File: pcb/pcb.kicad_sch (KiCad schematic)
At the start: 97 parts, among them J1 MJ-4PP-9, J2 MJ-4PP-9, J3 USB_C_Receptacle_USB2.0_16P, SW1 KEY_SW, SW10 KEY_SW, SW11 KEY_SW, SW12 KEY_SW, SW13 KEY_SW, SW14 KEY_SW, SW15 KEY_SW, SW16 KEY_SW, SW17 KEY_SW, SW18 KEY_SW, SW19 KEY_SW, SW2 KEY_SW, SW20 KEY_SW, SW21 KEY_SW, SW22 KEY_SW, SW23 KEY_SW, SW24 KEY_SW, SW25 KEY_SW, SW26 KEY_SW, SW27 RotaryEncoder, SW3 KEY_SW, SW30 KEY_SW, SW31 KEY_SW, SW32 KEY_SW, SW33 KEY_SW, SW34 KEY_SW, SW35 KEY_SW, SW36 KEY_SW, SW37 KEY_SW, SW38 KEY_SW, SW39 KEY_SW, SW4 KEY_SW, SW40 KEY_SW, SW41 KEY_SW, SW42 KEY_SW, SW43 KEY_SW, SW44 KEY_SW, SW45 KEY_SW, SW46 KEY_SW, SW47 KEY_SW, SW48 KEY_SW, SW49 KEY_SW, SW5 KEY_SW, SW50 KEY_SW, SW51 KEY_SW, SW52 KEY_SW, SW53 KEY_SW, SW54 KEY_SW, SW55 RotaryEncoder, SW6 KEY_SW, SW60 RESET_SW, SW61 BOOT_SW, SW7 KEY_SW, SW8 KEY_SW, SW9 KEY_SW, U1 ESP32-S3-WROOM-1, U2 TPS1117LV33S, U3 USBLC6-2SC6

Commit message: split connector close #8
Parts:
- added JP1: Jumper_2_Open, symbol Jumper:Jumper_2_Open
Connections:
- net +3V3: now also J2.D; no longer J2.C
- net GND: now also J2.C; no longer J2.D
- net at J1.A: now also J2.A, JP1.1 (A)
- net split-TX: now reaches J2.B
- net split-TX: now also J1.B, U1.10 (IO17)
- net split-RX: now reaches U1.11 (IO18)
- net split-RX: now also JP1.2 (B)
- removed net data: J1.B, J2.A
- no-connect marks 4 -> 3
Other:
- moved on the sheet: J1, J2

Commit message: pcb keyswitch
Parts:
- SW30: footprint keebio:RotaryEncoder_EC11 -> kbd:keyswitch_cherrymx_hotswap_1u
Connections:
- net col0: now also U1.39 (IO1)
- net col1: now also U1.38 (IO2)
- net col2: now also U1.15 (IO3)
- net col3: now also U1.4 (IO4)
- net col4: now also U1.5 (IO5)
- net col5: now also U1.6 (IO6)
- net col6: now also U1.7 (IO7)
- net row0: now also U1.31 (IO38)
- net row1: now also U1.32 (IO39)
- net row2: now also U1.33 (IO40)
- net row3: now also U1.34 (IO41)
- net USB-RX: now reaches U1.36 (RXD0)
- net USB-TX: now reaches U1.37 (TXD0)
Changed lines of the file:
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@@
     (stroke (width 0) (type default))
   )
+  (wire (pts (xy 110.49 197.485) (xy 111.76 197.485))
+    (stroke (width 0) (type default))
+  )
   (wire (pts (xy 260.35 100.33) (xy 260.35 120.65))
     (stroke (width 0) (type default))
@@
     (stroke (width 0) (type default))
   )
+  (wire (pts (xy 143.51 220.345) (xy 142.24 220.345))
+    (stroke (width 0) (type default))
+  )
   (wire (pts (xy 71.12 180.34) (xy 71.12 178.435))
     (stroke (width 0) (type default))
@@
     (stroke (width 0) (type default))
   )
+  (wire (pts (xy 110.49 205.105) (xy 111.76 205.105))
+    (stroke (width 0) (type default))
+  )
   (wire (pts (xy 184.15 68.58) (xy 184.15 88.9))
     (stroke (width 0) (type default))
@@
     (stroke (width 0) (type default))
   )
+  (wire (pts (xy 110.49 210.185) (xy 111.76 210.185))
+    (stroke (width 0) (type default))
+  )
+  (wire (pts (xy 143.51 217.805) (xy 142.24 217.805))
+    (stroke (width 0) (type default))
+  )
   (wire (pts (xy 199.39 107.95) (xy 224.79 107.95))
     (stroke (width 0) (type default))
@@
     (stroke (width 0) (type default))
   )
+  (wire (pts (xy 143.51 189.865) (xy 142.24 189.865))
+    (stroke (width 0) (type default))
+  )
   (wire (pts (xy 173.99 109.855) (xy 148.59 109.855))
     (stroke (width 0) (type default))
@@
     (stroke (width 0) (type default))
   )
+  (wire (pts (xy 143.51 222.885) (xy 142.24 222.885))
+    (stroke (width 0) (type default))
+  )
   (wire (pts (xy 250.19 44.45) (xy 275.59 44.45))
     (stroke (width 0) (type default))
@@
     (stroke (width 0) (type default))
   )
+  (wire (pts (xy 143.51 192.405) (xy 142.24 192.405))
+    (stroke (width 0) (type default))
+  )
   (wire (pts (xy 184.15 19.05) (xy 184.15 25.4))
     (stroke (width 0) (type default))
@@
     (stroke (width 0) (type default))
   )
+  (wire (pts (xy 110.49 200.025) (xy 111.76 200.025))
+    (stroke (width 0) (type default))
+  )
   (wire (pts (xy 45.085 199.39) (xy 48.895 199.39))
     (stroke (width 0) (type default))
@@
     (stroke (width 0) (type default))
   )
+  (wire (pts (xy 110.49 202.565) (xy 111.76 202.565))
+    (stroke (width 0) (type default))
+  )
   (wire (pts (xy 260.35 68.58) (xy 260.35 100.33))
     (stroke (width 0) (type default))
@@
     (stroke (width 0) (type default))
   )
+  (wire (pts (xy 110.49 207.645) (xy 111.76 207.645))
+    (stroke (width 0) (type default))
+  )
   (wire (pts (xy 143.51 129.54) (xy 143.51 130.175))
     (stroke (width 0) (type default))
@@
     (stroke (width 0) (type default))
   )
+  (wire (pts (xy 143.51 215.265) (xy 142.24 215.265))
+    (stroke (width 0) (type default))
+  )
   (wire (pts (xy 209.55 120.65) (xy 209.55 132.08))
     (stroke (width 0) (type default))
@@
     (stroke (width 0) (type default))
   )
+  (wire (pts (xy 110.49 212.725) (xy 111.76 212.725))
+    (stroke (width 0) (type default))
+  )
   (wire (pts (xy 133.35 68.58) (xy 133.35 88.9))
     (stroke (width 0) (type default))
@@
     )
   )
+  (global_label "col0" (shape input) (at 110.49 197.485 180) (fields_autoplaced)
+    (effects (font (size 1.27 1.27)) (justify right))
+    (property "Intersheetrefs" "${INTERSHEET_REFS}" (at 103.3925 197.485 0)
+      (effects (font (size 1.27 1.27)) (justify right) hide)
+    )
+  )
+  (global_label "USB-RX" (shape input) (at 143.51 192.405 0) (fields_autoplaced)
+    (effects (font (size 1.27 1.27)) (justify left))
+    (property "Intersheetrefs" "${INTERSHEET_REFS}" (at 154.3571 192.405 0)
+      (effects (font (size 1.27 1.27)) (justify left) hide)
+    )
+  )
   (global_label "row3" (shape output) (at 101.6 139.7 180) (fields_autoplaced)
     (effects (font (size 1.27 1.27)) (justify right))
@@
     )
   )
+  (global_label "col6" (shape input) (at 110.49 212.725 180) (fields_autoplaced)
+    (effects (font (size 1.27 1.27)) (justify right))
+    (property "Intersheetrefs" "${INTERSHEET_REFS}" (at 103.3925 212.725 0)
+      (effects (font (size 1.27 1.27)) (justify right) hide)
+    )
+  )
+  (global_label "row3" (shape input) (at 143.51 222.885 0) (fields_autoplaced)
+    (effects (font (size 1.27 1.27)) (justify left))
+    (property "Intersheetrefs" "${INTERSHEET_REFS}" (at 150.9704 222.885 0)
+      (effects (font (size 1.27 1.27)) (justify left) hide)
+    )
+  )
+  (global_label "row1" (shape input) (at 143.51 217.805 0) (fields_autoplaced)
+    (effects (font (size 1.27 1.27)) (justify left))
+    (property "Intersheetrefs" "${INTERSHEET_REFS}" (at 150.9704 217.805 0)
+      (effects (font (size 1.27 1.27)) (justify left) hide)
+    )
+  )
   (global_label "col6" (shape output) (at 260.35 19.05 90) (fields_autoplaced)
     (effects (font (size 1.27 1.27)) (justify left))
@@
     )
   )
+  (global_label "col2" (shape input) (at 110.49 202.565 180) (fields_autoplaced)
+    (effects (font (size 1.27 1.27)) (justify right))
+    (property "Intersheetrefs" "${INTERSHEET_REFS}" (at 103.3925 202.565 0)
+      (effects (font (size 1.27 1.27)) (justify right) hide)
+    )
+  )
   (global_label "rotaryA" (shape output) (at 142.875 109.855 180) (fields_autoplaced)
     (effects (font (size 1.27 1.27)) (justify right))
@@
     )
   )
+  (global_label "col3" (shape input) (at 110.49 205.105 180) (fields_autoplaced)
+    (effects (font (size 1.27 1.27)) (justify right))
+    (property "Intersheetrefs" "${INTERSHEET_REFS}" (at 103.3925 205.105 0)
+      (effects (font (size 1.27 1.27)) (justify right) hide)
+    )
+  )
+  (global_label "col5" (shape input) (at 110.49 210.185 180) (fields_autoplaced)
+    (effects (font (size 1.27 1.27)) (justify right))
+    (property "Intersheetrefs" "${INTERSHEET_REFS}" (at 103.3925 210.185 0)
+      (effects (font (size 1.27 1.27)) (justify right) hide)
+    )
+  )
   (global_label "split-RX" (shape input) (at 260.985 174.625 0) (fields_autoplaced)
     (effects (font (size 1.27 1.27)) (justify left))
@@
     )
   )
+  (global_label "USB-TX" (shape output) (at 143.51 189.865 0) (fields_autoplaced)
+    (effects (font (size 1.27 1.27)) (justify left))
+    (property "Intersheetrefs" "${INTERSHEET_REFS}" (at 154.0547 189.865 0)
+      (effects (font (size 1.27 1.27)) (justify left) hide)
+    )
+  )
+  (global_label "col1" (shape input) (at 110.49 200.025 180) (fields_autoplaced)
+    (effects (font (size 1.27 1.27)) (justify right))
+    (property "Intersheetrefs" "${INTERSHEET_REFS}" (at 103.3925 200.025 0)
+      (effects (font (size 1.27 1.27)) (justify right) hide)
+    )
+  )
   (global_label "col1" (shape output) (at 133.35 19.05 90) (fields_autoplaced)
     (effects (font (size 1.27 1.27)) (justify left))
@@
     )
   )
+  (global_label "col4" (shape input) (at 110.49 207.645 180) (fields_autoplaced)
+    (effects (font (size 1.27 1.27)) (justify right))
+    (property "Intersheetrefs" "${INTERSHEET_REFS}" (at 103.3925 207.645 0)
+      (effects (font (size 1.27 1.27)) (justify right) hide)
+    )
+  )
   (global_label "rotaryB" (shape output) (at 142.875 112.395 180) (fields_autoplaced)
     (effects (font (size 1.27 1.27)) (justify right))
@@
     )
   )
+  (global_label "row0" (shape input) (at 143.51 215.265 0) (fields_autoplaced)
+    (effects (font (size 1.27 1.27)) (justify left))
+    (property "Intersheetrefs" "${INTERSHEET_REFS}" (at 150.9704 215.265 0)
+      (effects (font (size 1.27 1.27)) (justify left) hide)
+    )
+  )
+  (global_label "row2" (shape input) (at 143.51 220.345 0) (fields_autoplaced)
+    (effects (font (size 1.27 1.27)) (justify left))
+    (property "Intersheetrefs" "${INTERSHEET_REFS}" (at 150.9704 220.345 0)
+      (effects (font (size 1.27 1.27)) (justify left) hide)
+    )
+  )
   (global_label "col3" (shape output) (at 184.15 19.05 90) (fields_autoplaced)
     (effects (font (size 1.27 1.27)) (justify left))
@@
     )
     (property "Footprint" "" (at 88.9 202.565 0)
-      (effects (font (size 1.27 1.27)))
+      (effects (font (size 1.27 1.27)) hide)
     )
     (property "Datasheet" "" (at 88.9 202.565 0)
@@
       (effects (font (size 1.27 1.27)))
     )
-    (property "Footprint" "keebio:RotaryEncoder_EC11" (at 115.57 25.4 0)
+    (property "Footprint" "kbd:keyswitch_cherrymx_hotswap_1u" (at 115.57 25.4 0)
       (effects (font (size 1.27 1.27)) hide)
     )

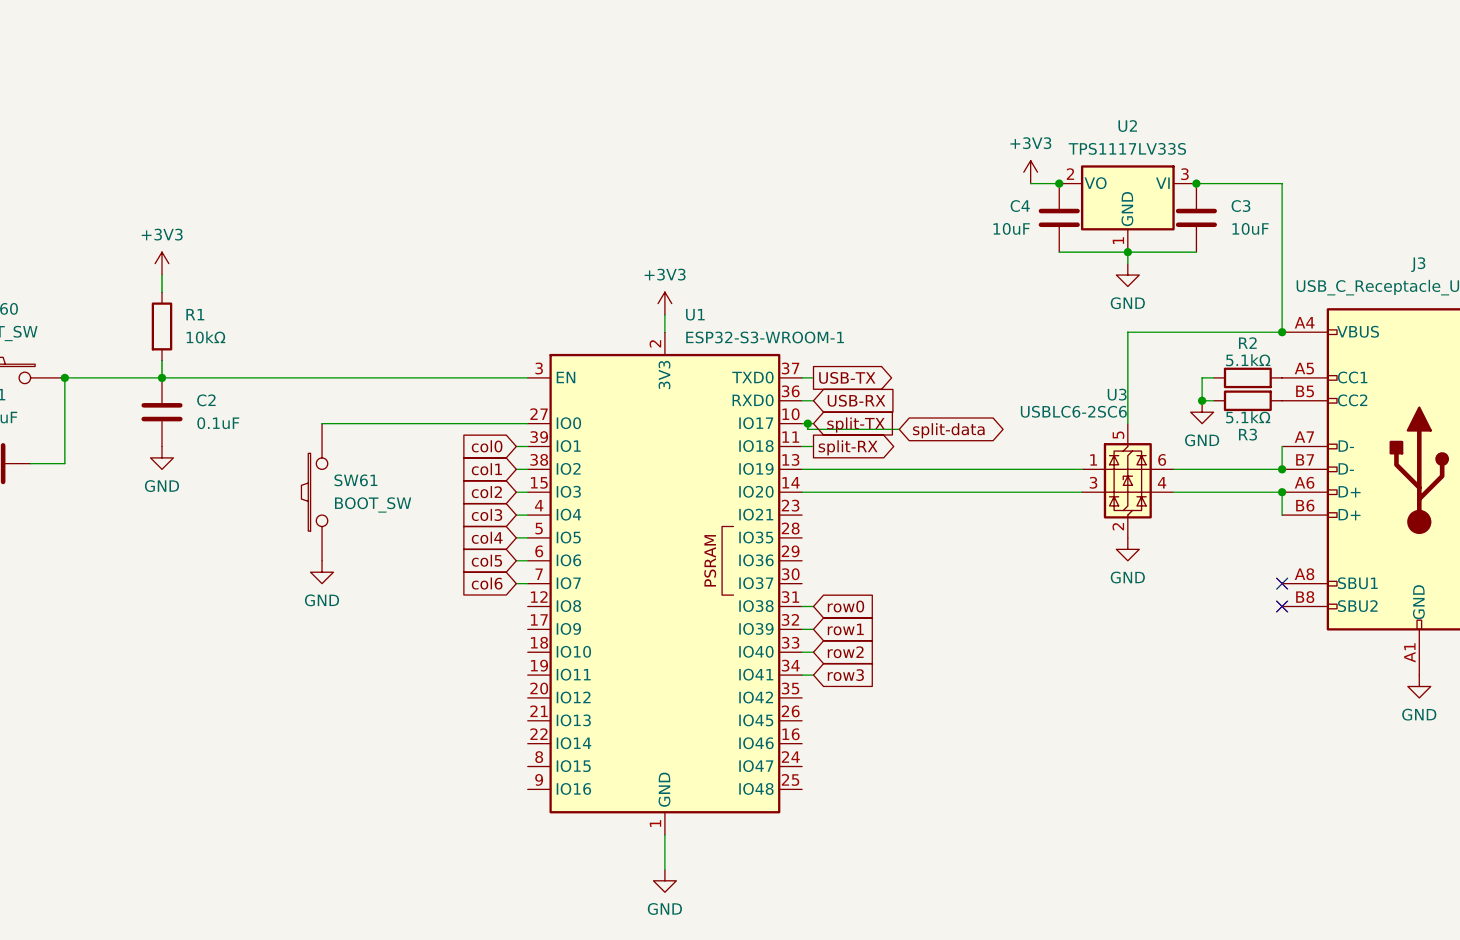
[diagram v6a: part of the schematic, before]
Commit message: USB to TTL close #9
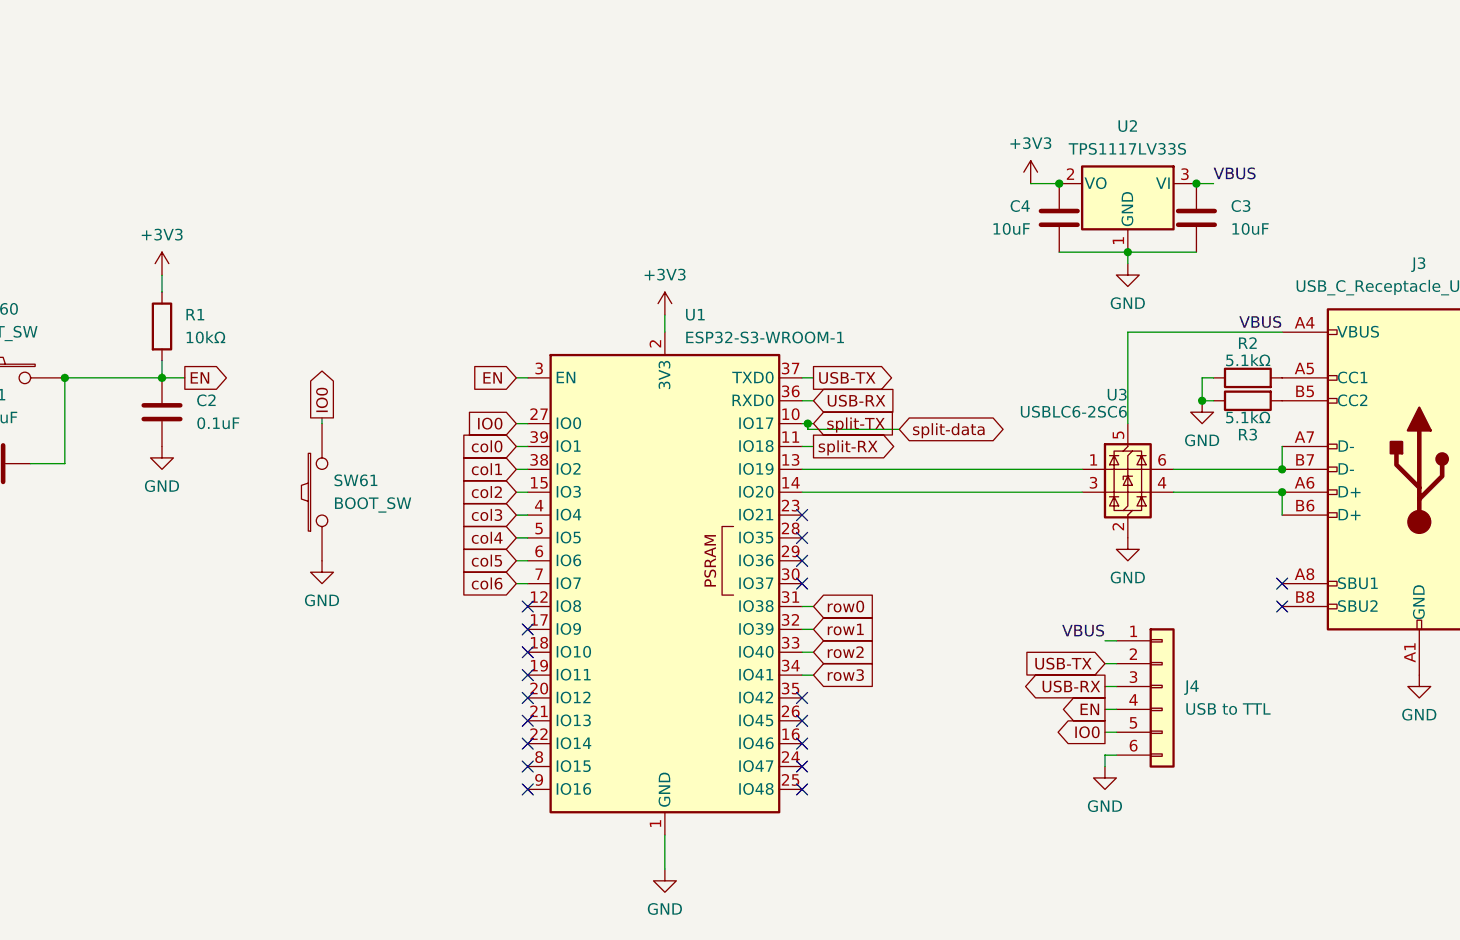
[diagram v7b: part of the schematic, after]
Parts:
- added J4: USB to TTL, Connector_PinSocket_2.54mm:PinSocket_1x06_P2.54mm_Horizontal, symbol Connector_Generic:Conn_01x06
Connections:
- net GND: now also J4.6 (Pin_6)
- net USB-RX: now also J4.3 (Pin_3)
- net USB-TX: now also J4.2 (Pin_2)
- net EN: now reaches C1.2, C2.2, R1.2, SW60.2, U1.3 (EN)
- net EN: now also J4.4 (Pin_4)
- net VBUS: now reaches C3.1, J3.A4 (VBUS), J3.A9 (VBUS), J3.B4 (VBUS), J3.B9 (VBUS), U2.3 (VI), U3.5 (VBUS)
- net VBUS: now also J4.1 (Pin_1)
- net IO0: now reaches SW61.2, U1.27 (IO0)
- net IO0: now also J4.5 (Pin_5)
- no-connect marks 3 -> 21

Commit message: DIP SW close #15
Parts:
- removed JP1: Jumper_2_Open, symbol Jumper:Jumper_2_Open
- added SW62: DIP_SW, lib:DIPS762W80P254L1170H690Q8N, symbol Switch:SW_DIP_x04
- J3: footprint (none) -> Connector_USB:USB_C_Receptacle_GCT_USB4105-xx-A_16P_TopMnt_Horizontal
- R1, R2, R3, R4: footprint (none) -> keebio:Resistor-Hybrid
- SW60, SW61: footprint (none) -> kbd:ResetSW
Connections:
- net GND: now also SW62.2, SW62.3, SW62.4
- net split-RX: now also SW62.8
- net split toggle: now reaches J1.A, J2.A
- net split toggle: now also SW62.1
- net power toggle: now reaches U1.12 (IO8)
- net power toggle: now also SW62.7
- net BLE toggle: now reaches U1.17 (IO9)
- net BLE toggle: now also SW62.6
- net LED toggle: now reaches U1.18 (IO10)
- net LED toggle: now also SW62.5
- no-connect marks 21 -> 16
